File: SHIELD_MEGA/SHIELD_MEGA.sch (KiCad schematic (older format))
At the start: 1 part

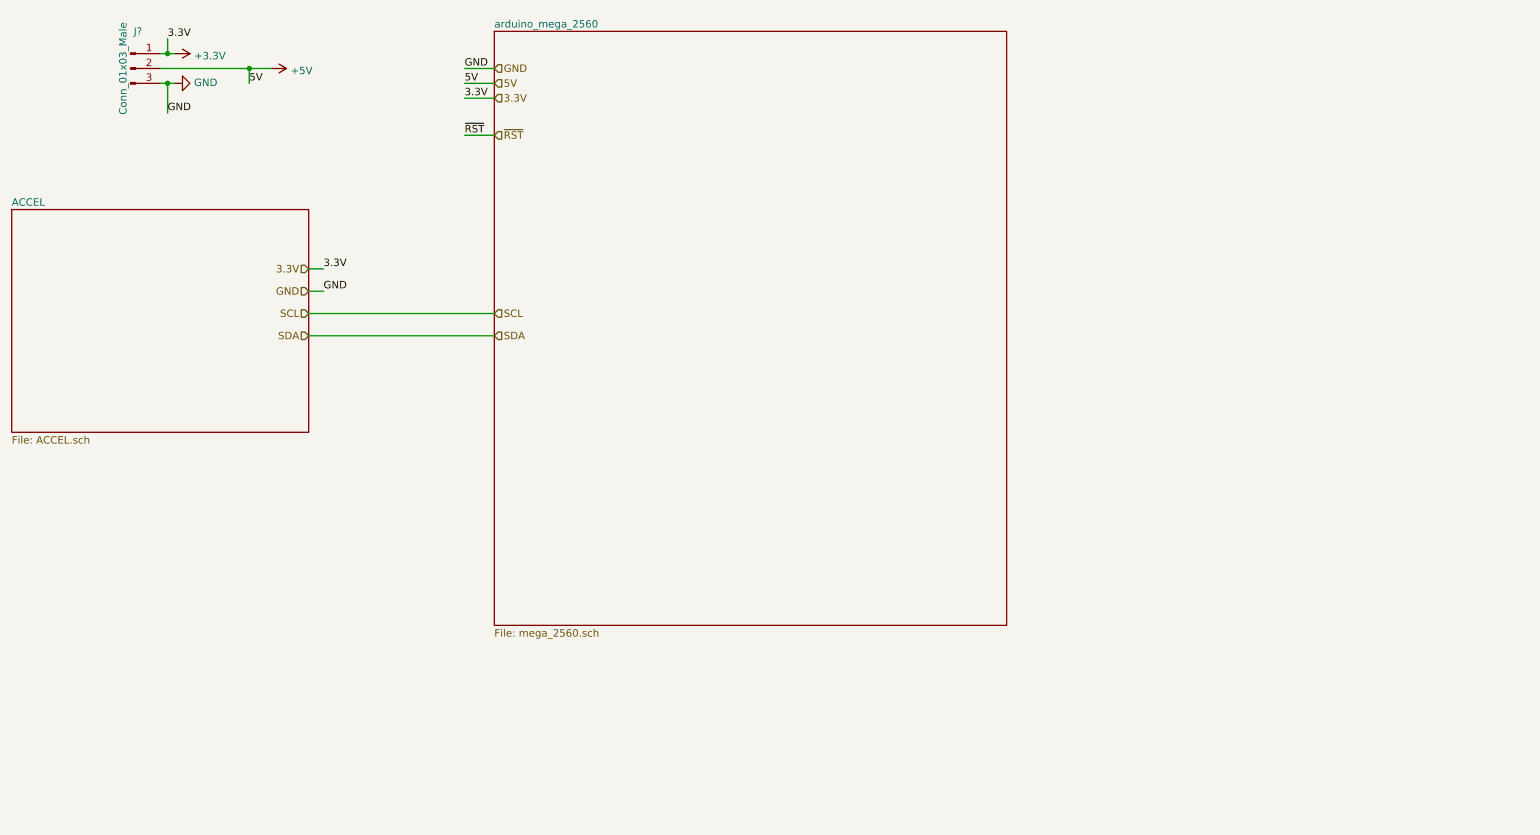
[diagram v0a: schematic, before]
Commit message: Updating arduino mega schematic main page
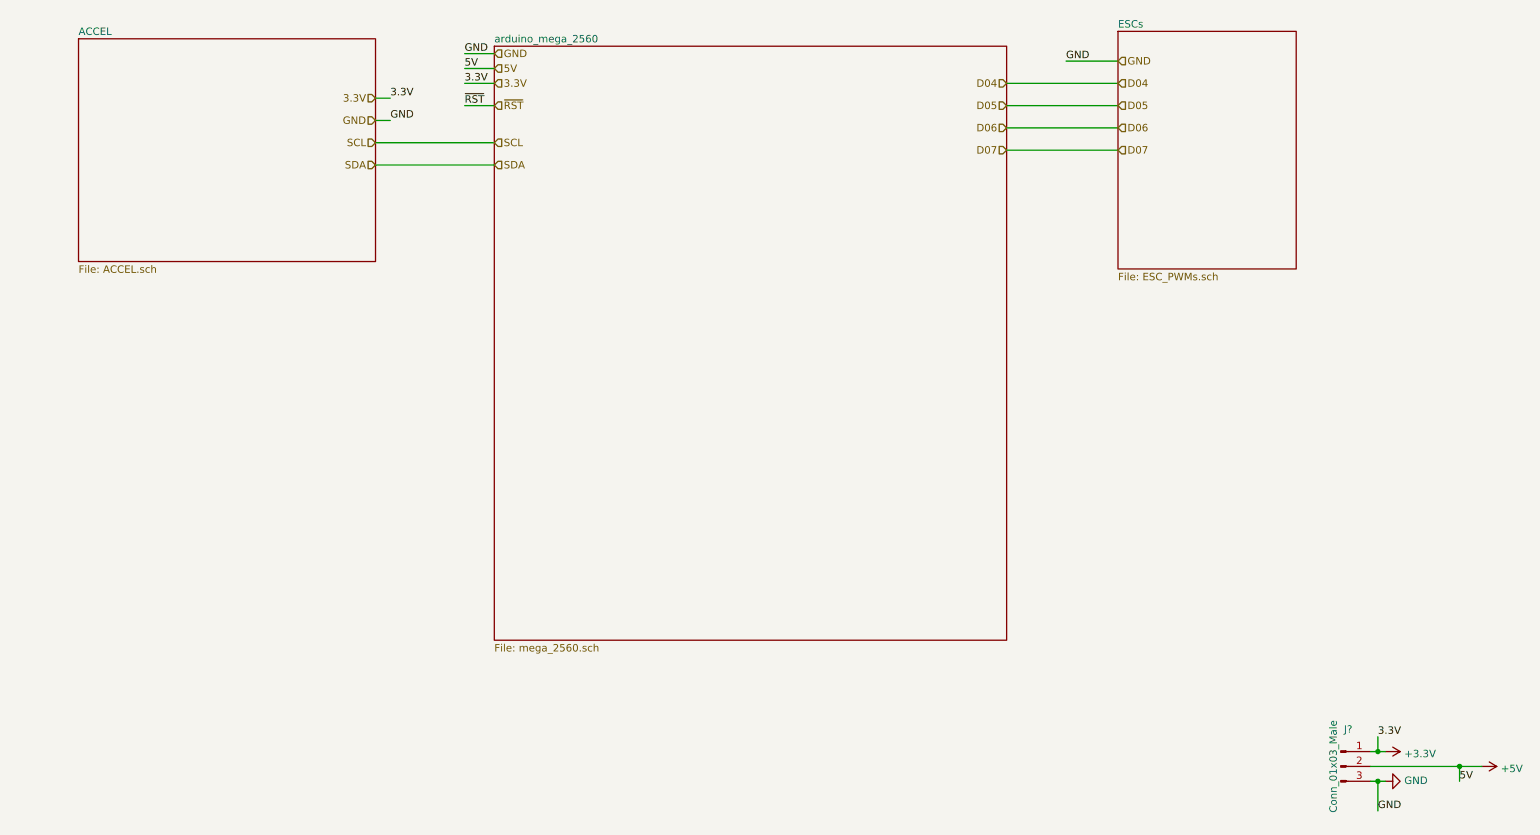
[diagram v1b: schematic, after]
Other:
- moved on the sheet: J?
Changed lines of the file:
@@
 $Descr A4 11693 8268
 encoding utf-8
-Sheet 1 3
+Sheet 1 4
 Title ""
 Date ""
@@
 $EndDescr
 $Sheet
-S 4050 1000 3450 4000
+S 4050 1100 3450 4000
 U 6194FDB3
 F0 "arduino_mega_2560" 50
@@
 L Connector:Conn_01x03_Male J?
 U 1 1 61954CC1
-P 1600 1250
-F 0 "J?" H 1650 1500 50  0000 C CNN
-F 1 "Conn_01x03_Male" V 1550 1250 50  0000 C CNN
-F 2 "" H 1600 1250 50  0001 C CNN
-F 3 "~" H 1600 1250 50  0001 C CNN
-	1    1600 1250
+P 9750 5950
+F 0 "J?" H 9800 6200 50  0000 C CNN
+F 1 "Conn_01x03_Male" V 9700 5950 50  0000 C CNN
+F 2 "" H 9750 5950 50  0001 C CNN
+F 3 "~" H 9750 5950 50  0001 C CNN
+	1    9750 5950
 	1    0    0    -1
 $EndComp
@@
 L power:+3.3V #PWR?
 U 1 1 6195629E
-P 1900 1150
-F 0 "#PWR?" H 1900 1000 50  0001 C CNN
-F 1 "+3.3V" V 1915 1278 50  0000 L CNN
-F 2 "" H 1900 1150 50  0001 C CNN
-F 3 "" H 1900 1150 50  0001 C CNN
-	1    1900 1150
+P 10050 5850
+F 0 "#PWR?" H 10050 5700 50  0001 C CNN
+F 1 "+3.3V" V 10065 5978 50  0000 L CNN
+F 2 "" H 10050 5850 50  0001 C CNN
+F 3 "" H 10050 5850 50  0001 C CNN
+	1    10050 5850
 	0    1    1    0
 $EndComp
@@
 L power:+5V #PWR?
 U 1 1 61956DDE
-P 2550 1250
-F 0 "#PWR?" H 2550 1100 50  0001 C CNN
-F 1 "+5V" V 2565 1378 50  0000 L CNN
-F 2 "" H 2550 1250 50  0001 C CNN
-F 3 "" H 2550 1250 50  0001 C CNN
-	1    2550 1250
+P 10700 5950
+F 0 "#PWR?" H 10700 5800 50  0001 C CNN
+F 1 "+5V" V 10715 6078 50  0000 L CNN
+F 2 "" H 10700 5950 50  0001 C CNN
+F 3 "" H 10700 5950 50  0001 C CNN
+	1    10700 5950
 	0    1    1    0
 $EndComp
@@
 L power:GND #PWR?
 U 1 1 6195741C
-P 1900 1350
-F 0 "#PWR?" H 1900 1100 50  0001 C CNN
-F 1 "GND" V 1905 1222 50  0000 R CNN
-F 2 "" H 1900 1350 50  0001 C CNN
-F 3 "" H 1900 1350 50  0001 C CNN
-	1    1900 1350
+P 10050 6050
+F 0 "#PWR?" H 10050 5800 50  0001 C CNN
+F 1 "GND" V 10055 5922 50  0000 R CNN
+F 2 "" H 10050 6050 50  0001 C CNN
+F 3 "" H 10050 6050 50  0001 C CNN
+	1    10050 6050
 	0    -1   -1   0
 $EndComp
 Wire Wire Line
-	1800 1150 1850 1150
+	9950 5850 10000 5850
 Wire Wire Line
-	1800 1250 2400 1250
+	9950 5950 10550 5950
 Wire Wire Line
-	1800 1350 1850 1350
-Text HLabel 4050 1250 2    50   Input ~ 0
+	9950 6050 10000 6050
+Text HLabel 4050 1150 2    50   Input ~ 0
 GND
-Text Label 3850 1250 0    50   ~ 0
+Text Label 3850 1150 0    50   ~ 0
 GND
 Wire Wire Line
-	3850 1250 4050 1250
+	3850 1150 4050 1150
 Wire Wire Line
-	1850 1550 1850 1350
-Connection ~ 1850 1350
+	10000 6250 10000 6050
+Connection ~ 10000 6050
 Wire Wire Line
-	1850 1350 1900 1350
-Text Label 1850 1550 0    50   ~ 0
+	10000 6050 10050 6050
+Text Label 10000 6250 0    50   ~ 0
 GND
-Text Label 2400 1350 0    50   ~ 0
+Text Label 10550 6050 0    50   ~ 0
 5V
 Wire Wire Line
-	2400 1350 2400 1250
-Connection ~ 2400 1250
+	10550 6050 10550 5950
+Connection ~ 10550 5950
 Wire Wire Line
-	2400 1250 2550 1250
-Text Label 1850 1050 0    50   ~ 0
+	10550 5950 10700 5950
+Text Label 10000 5750 0    50   ~ 0
 3.3V
 Wire Wire Line
-	1850 1050 1850 1150
-Connection ~ 1850 1150
+	10000 5750 10000 5850
+Connection ~ 10000 5850
 Wire Wire Line
-	1850 1150 1900 1150
-Text HLabel 4050 1450 2    50   Input ~ 0
+	10000 5850 10050 5850
+Text HLabel 4050 1350 2    50   Input ~ 0
 3.3V
-Text HLabel 4050 1350 2    50   Input ~ 0
+Text HLabel 4050 1250 2    50   Input ~ 0
 5V
 Wire Wire Line
+	4050 1250 3850 1250
+Wire Wire Line
 	4050 1350 3850 1350
-Wire Wire Line
-	4050 1450 3850 1450
+Text Label 3850 1250 0    50   ~ 0
+5V
 Text Label 3850 1350 0    50   ~ 0
-5V
-Text Label 3850 1450 0    50   ~ 0
 3.3V
-Text HLabel 4050 1700 2    50   Input ~ 0
+Text HLabel 4050 1500 2    50   Input ~ 0
 ~RST
-Text Label 3850 1700 0    50   ~ 0
+Text Label 3850 1500 0    50   ~ 0
 ~RST
 Wire Wire Line
-	3850 1700 4050 1700
+	3850 1500 4050 1500
 $Sheet
-S 800  2200 2000 1500
+S 1250 1050 2000 1500
 U 619602F2
 F0 "ACCEL" 50
 F1 "ACCEL.sch" 50
 $EndSheet
-Text HLabel 2800 2600 0    50   Input ~ 0
+Text HLabel 3250 1450 0    50   Input ~ 0
 3.3V
-Text HLabel 2800 2750 0    50   Input ~ 0
+Text HLabel 3250 1600 0    50   Input ~ 0
 GND
-Text HLabel 2800 2900 0    50   Input ~ 0
+Text HLabel 3250 1750 0    50   Input ~ 0
 SCL
-Text HLabel 2800 3050 0    50   Input ~ 0
+Text HLabel 3250 1900 0    50   Input ~ 0
 SDA
 Wire Wire Line
-	2800 2600 2900 2600
-Text Label 2900 2600 0    50   ~ 0
+	3250 1450 3350 1450
+Text Label 3350 1450 0    50   ~ 0
 3.3V
-Text Label 2900 2750 0    50   ~ 0
+Text Label 3350 1600 0    50   ~ 0
 GND
 Wire Wire Line
-	2900 2750 2800 2750
-Text HLabel 4050 2900 2    50   Input ~ 0
+	3350 1600 3250 1600
+Text HLabel 4050 1750 2    50   Input ~ 0
 SCL
-Text HLabel 4050 3050 2    50   Input ~ 0
+Text HLabel 4050 1900 2    50   Input ~ 0
 SDA
+Text HLabel 8250 1200 2    50   Input ~ 0
+GND
+$Sheet
+S 8250 1000 1200 1600
+U 619656BE
+F0 "ESCs" 50
+F1 "ESC_PWMs.sch" 50
+$EndSheet
+Text HLabel 8250 1350 2    50   Input ~ 0
+D04
+Text HLabel 8250 1500 2    50   Input ~ 0
+D05
+Text HLabel 8250 1650 2    50   Input ~ 0
+D06
+Text HLabel 8250 1800 2    50   Input ~ 0
+D07
 Wire Wire Line
-	2800 2900 4050 2900
+	3250 1750 4050 1750
 Wire Wire Line
-	2800 3050 4050 3050
+	4050 1900 3250 1900
+Text Label 7900 1200 0    50   ~ 0
+GND
+Wire Wire Line
+	7900 1200 8250 1200
+Text HLabel 7500 1350 0    50   Input ~ 0
+D04
+Text HLabel 7500 1500 0    50   Input ~ 0
+D05
+Text HLabel 7500 1650 0    50   Input ~ 0
+D06
+Text HLabel 7500 1800 0    50   Input ~ 0
+D07
+Wire Wire Line
+	7500 1800 8250 1800
+Wire Wire Line
+	8250 1650 7500 1650
+Wire Wire Line
+	7500 1500 8250 1500
+Wire Wire Line
+	8250 1350 7500 1350
 $EndSCHEMATC
